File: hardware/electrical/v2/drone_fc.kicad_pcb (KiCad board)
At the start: 4 copper layers, 30 x 40.8 mm, 37 parts, among them J1 Cortex_SWD_10P, J2 ESC_4IN1_JST_SH, U1 TLV75533PDBVR, U2 LMR50410_Buck, U3 MDBT53-P1M, U4 ICM-42688-P

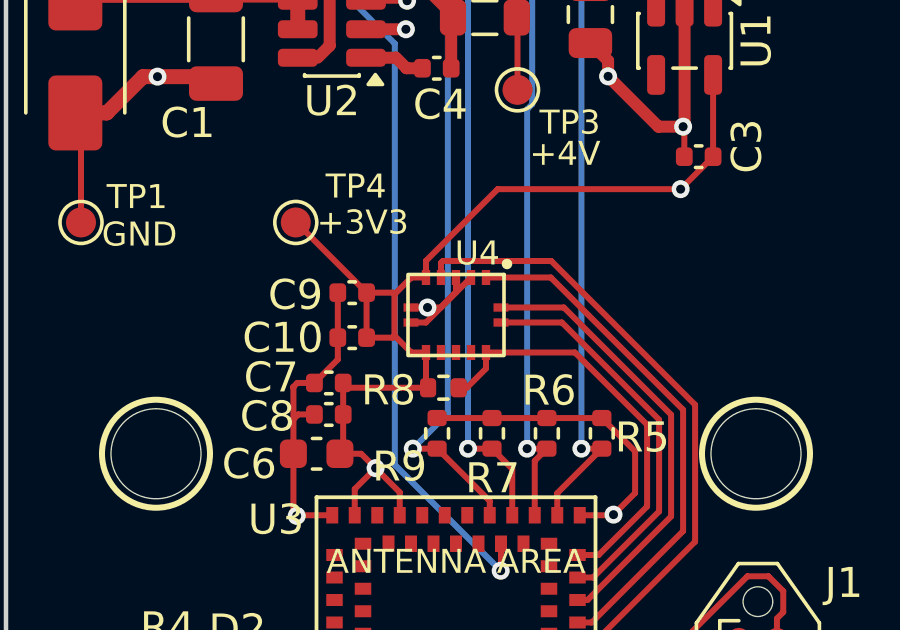
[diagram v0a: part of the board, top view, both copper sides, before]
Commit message: u4: fix ICM-42688-P footprint pad layout to match the datasheet
Pins 5 and 12 were placed as a 5th pad on the left/right edges
instead of on the bottom/top edges, giving a 5-5-2-2 pad distribution
across the four sides instead of the correct 4-3-4-3 (per Figure 5,
the pin-out diagram in DS-000347 rev 1.6, page 20). Text-extracting
the datasheet's pin table alone didn't catch this - it only confirmed
pin numbers map to the right signal names, not that the physical pad
positions matched the package outline. Rendering the actual diagram
page as an image caught the mismatch.

Moves pin 5 (VDDIO) onto the bottom edge and pin 12 (AP_CS) onto the
top edge, each at the correct 0.5 mm pitch alongside pins 6/7 and
13/14. Board re-routed for the two moved pads, including a GND via
that had ended up too close to the relocated pad 5.

ERC clean, DRC clean (0 errors, 0 unconnected).
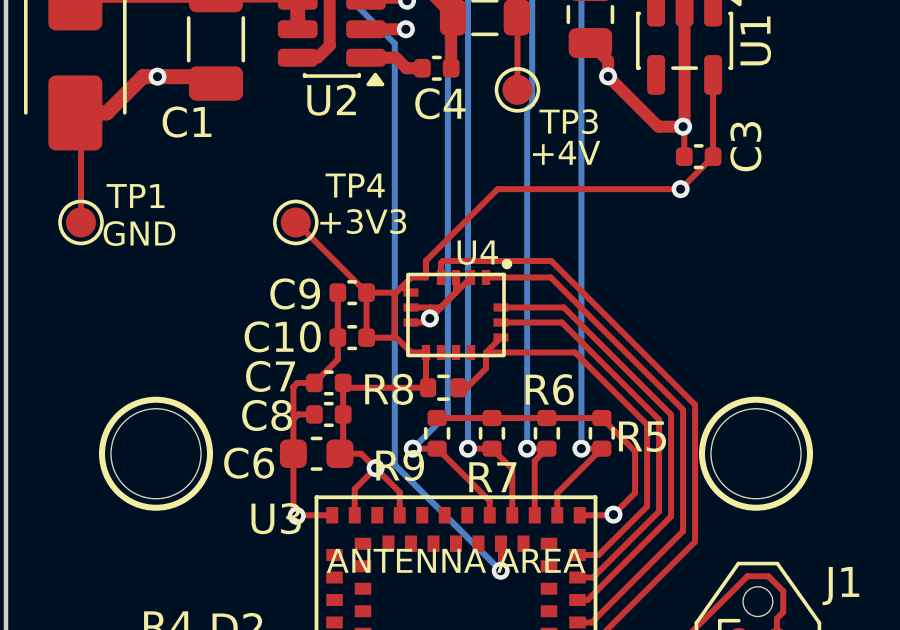
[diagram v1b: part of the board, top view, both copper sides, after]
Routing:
- net GND: track 69.5 -> 70.2 mm
- net /IMU_CS: track 13.8 -> 14.5 mm
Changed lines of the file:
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@@
 		(sheetname "/")
 		(sheetfile "drone_fc.kicad_sch")
-		(units
-			(unit
-				(name "A")
-				(pins "13" "1" "14" "12" "4" "9" "8" "5" "11" "2" "6" "7" "3" "10")
-			)
-		)
 		(attr smd)
 		(duplicate_pad_numbers_are_jumpers no)
@@
 		)
 		(pad "5" smd rect
-			(at -1.25 1 270)
-			(size 0.5 0.28)
+			(at -0.75 1.5 270)
+			(size 0.28 0.5)
 			(layers "F.Cu" "F.Mask" "F.Paste")
 			(net "/+3V3")
@@
 		)
 		(pad "12" smd rect
-			(at 1.25 -1 270)
-			(size 0.5 0.28)
+			(at 0.75 -1.5 270)
+			(size 0.28 0.5)
 			(layers "F.Cu" "F.Mask" "F.Paste")
 			(net "/IMU_CS")
@@
 	)
 	(segment
-		(start 98.5 105.125)
-		(end 99.05 105.125)
+		(start 94.57 107.78)
+		(end 94.58 107.79)
 		(width 0.2)
 		(layer "F.Cu")
@@
 	)
 	(segment
-		(start 94.57 107.78)
-		(end 94.58 107.79)
+		(start 99.49 105.12919)
+		(end 99.12919 105.49)
 		(width 0.2)
 		(layer "F.Cu")
@@
 	)
 	(segment
-		(start 100 104.615)
-		(end 100 104.125)
-		(width 0.2)
-		(layer "F.Cu")
-		(net "GND")
-	)
-	(segment
 		(start 94.74 108.69)
 		(end 94.58 108.85)
@@
 	)
 	(segment
-		(start 99.49 105.125)
-		(end 100 104.615)
+		(start 100 104.615)
+		(end 100 104.125)
 		(width 0.2)
 		(layer "F.Cu")
@@
 	)
 	(segment
+		(start 98.5 105.125)
+		(end 99.12919 105.125)
+		(width 0.2)
+		(layer "F.Cu")
+		(net "GND")
+	)
+	(segment
 		(start 96.06 106.13)
 		(end 96.06 104.63)
@@
 	)
 	(segment
+		(start 99.49 105.125)
+		(end 100 104.615)
+		(width 0.2)
+		(layer "F.Cu")
+		(net "GND")
+	)
+	(segment
 		(start 89.87 116.88)
 		(end 89.87 119.39)
@@
 	)
 	(segment
+		(start 99.49 105.125)
+		(end 99.49 105.12919)
+		(width 0.2)
+		(layer "F.Cu")
+		(net "GND")
+	)
+	(segment
 		(start 104.125 112.05)
 		(end 105.23 112.05)
@@
 	)
 	(segment
-		(start 99.05 105.125)
-		(end 99.49 105.125)
+		(start 94.58 110)
+		(end 94.58 111.96)
 		(width 0.2)
 		(layer "F.Cu")
@@
 	)
 	(segment
-		(start 94.58 110)
-		(end 94.58 111.96)
+		(start 99.12919 105.125)
+		(end 99.49 105.125)
 		(width 0.2)
 		(layer "F.Cu")
@@
 	)
 	(via
-		(at 99.05 105.125)
+		(at 105.31 121.25)
 		(size 0.6)
 		(drill 0.3)
@@
 	)
 	(via
-		(at 105.31 121.25)
+		(at 105.25 112.03)
 		(size 0.6)
 		(drill 0.3)
@@
 	)
 	(via
-		(at 105.25 112.03)
+		(at 99.12919 105.49)
 		(size 0.6)
 		(drill 0.3)
@@
 	)
 	(segment
+		(start 99.12919 105.49)
+		(end 99.32919 105.49)
+		(width 0.2)
+		(layer "B.Cu")
+		(net "GND")
+	)
+	(segment
 		(start 99 107.73)
 		(end 99 106.625)
@@
 	(segment
 		(start 98.51 104.125)
-		(end 97.95 104.685)
+		(end 98.2125 104.4225)
 		(width 0.2)
 		(layer "F.Cu")
@@
 	)
 	(segment
+		(start 98.5 104.625)
+		(end 98.415 104.625)
+		(width 0.2)
+		(layer "F.Cu")
+		(net "/+3V3")
+	)
+	(segment
 		(start 97.02 104.63)
 		(end 97.895 104.63)
@@
 		(net "/+3V3")
 	)
+	(segment
+		(start 98.415 104.625)
+		(end 98.2125 104.4225)
+		(width 0.2)
+		(layer "F.Cu")
+		(net "/+3V3")
+	)
+	(segment
+		(start 98.2125 104.4225)
+		(end 97.95 104.685)
+		(width 0.2)
+		(layer "F.Cu")
+		(net "/+3V3")
+	)
 	(via
 		(at 107.487556 101.18)
@@
 		(width 0.2)
 		(layer "F.Cu")
+		(net "/IMU_CS")
+	)
+	(segment
+		(start 101.5 106.125)
+		(end 101 106.625)
+		(width 0.2)
+		(layer "F.Cu")

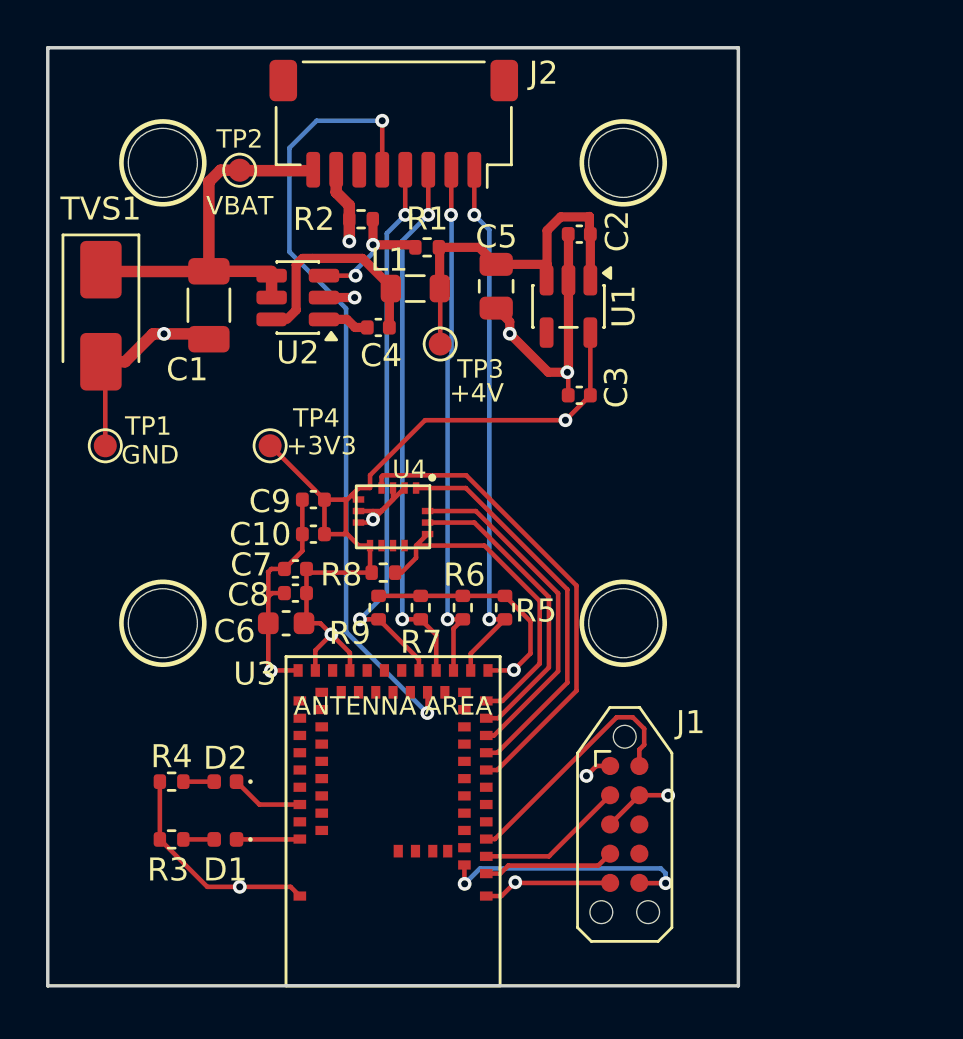
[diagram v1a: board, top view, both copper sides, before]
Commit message: u4: re-center IMU footprint pads and add a 3D model
Pin rows were shifted 0.25 mm off the package centerline on all four
edges (e.g. the left edge read -1.00/-0.50/0.00/+0.50 instead of the
symmetric -0.75/-0.25/+0.25/+0.75 a 0.5 mm pitch, 4-pin edge should
have). Found by rendering the mechanical drawing on page 55 of the
datasheet (DS-000347 rev 1.6) and comparing directly, rather than
trusting the pin-function table alone. Outer edge offsets (+-1.25 mm,
+-1.5 mm) already matched the 2.5x3.0 mm package half-dimensions and
were untouched.

Also adds a 3D model: no vendor STEP exists for the ICM-42688-P, so
this references KiCad's bundled generic LGA-14 3x2.5mm P0.5mm body
(Package_LGA.3dshapes, LayoutBorder3x4y - 3 pins on the short edges,
4 on the long edges, matching this part's pinout), rotated 90 degrees
to align its long axis with ours. Confirmed by render.

Board re-routed for the pad shift; a GND via that ended up too close
to the relocated pad 5 was moved clear. ERC clean, DRC clean (0
errors, 0 unconnected).
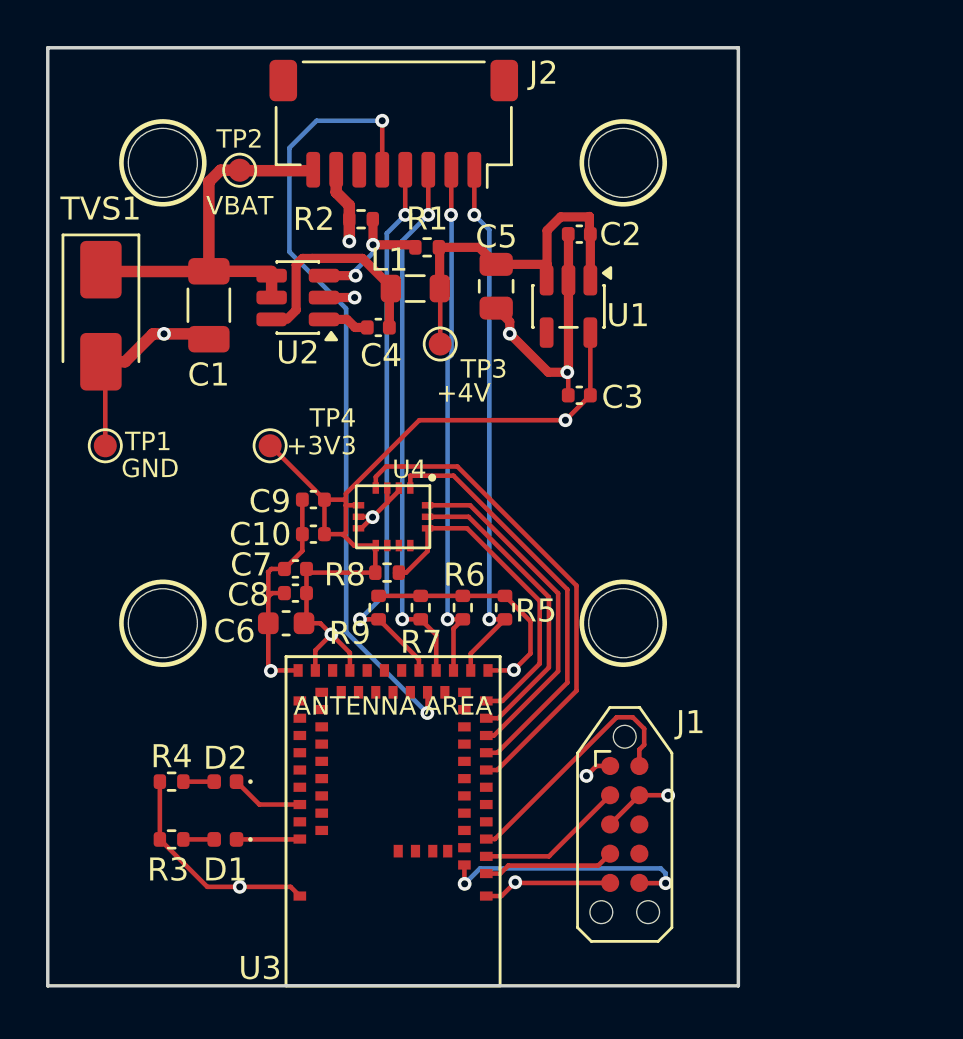
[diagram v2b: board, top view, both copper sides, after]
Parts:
- moved R8 0.16 mm to (99.7, 107.8)
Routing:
- net GND: track 70.2 -> 68.6 mm
- net /SPI_MISO: track 17.2 -> 18.2 mm
- net /IMU_INT1: track 20.9 -> 21.4 mm

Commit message: layout: add silkscreen text
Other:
- board text added: "${PROJECTNAME}"
- board text added: "NRP"
- board text added: "RADIO"
- board text added: "STATUS"
- board text added: "v1.0"
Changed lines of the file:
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@@
 		(layer "Edge.Cuts")
+	)
+	(gr_text "RADIO"
+		(at 89.39 114.95 0)
+		(layer "F.Cu")
+		(effects
+			(font
+				(size 1 1)
+				(thickness 0.15)
+				(bold yes)
+			)
+			(justify left bottom)
+		)
+	)
+	(gr_text ""
+		(at 108.2 104.99 0)
+		(layer "F.Cu")
+		(effects
+			(font
+				(size 1 1)
+				(thickness 0.15)
+				(bold yes)
+			)
+			(justify left bottom)
+		)
+	)
+	(gr_text "${PROJECTNAME}"
+		(at 107.94 103.59 0)
+		(layer "F.SilkS")
+		(effects
+			(font
+				(size 1 1)
+				(thickness 0.1)
+			)
+			(justify left bottom)
+		)
+	)
+	(gr_text "v1.0"
+		(at 107.94 105.065 0)
+		(layer "F.SilkS")
+		(effects
+			(font
+				(size 1 1)
+				(thickness 0.1)
+			)
+			(justify left bottom)
+		)
+	)
+	(gr_text "NRP"
+		(at 107.94 106.54 0)
+		(layer "F.SilkS")
+		(effects
+			(font
+				(size 1 1)
+				(thickness 0.1)
+			)
+			(justify left bottom)
+		)
+	)
+	(gr_text "STATUS"
+		(at 89.23 123.25 0)
+		(layer "F.SilkS")
+		(effects
+			(font
+				(size 1 1)
+				(thickness 0.15)
+				(bold yes)
+			)
+			(justify left bottom)
+		)
 	)
 	(segment

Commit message: hardware: sync PCB symbols and correct LED orientation
Apply the standard symbols and complete module pin metadata to the PCB. Rotate both LEDs to match their corrected polarity, move RADIO to silkscreen, and update the revision marking to v2.1.

Track, via and zone geometry is unchanged. Refilled-zone DRC finds no unconnected pads; only the existing silkscreen and mounting-hole warnings remain. Preserve the previously exported manufacturing files.
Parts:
- moved D1 0.06 mm to (92.7, 119.5), turned to 0 degrees
- turned D2 to 0 degrees
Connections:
- D1 pad 1: Net-(D1-A) -> Net-(D1-K)
- D1 pad 2: Net-(D1-K) -> /LED_STATUS
- D2 pad 1: Net-(D2-A) -> Net-(D2-K)
- D2 pad 2: Net-(D2-K) -> /LED_RADIO
- J1 pad 7: (no net) -> unconnected-(J1-KEY-Pad7)
- J1 pad 8: (no net) -> unconnected-(J1-NC/TDI-Pad8)
- U3 pad 10: (no net) -> unconnected-(U3B-P1.06-Pad10)
- U3 pad 11: (no net) -> unconnected-(U3B-P1.04-Pad11)
- U3 pad 12: (no net) -> unconnected-(U3B-P0.21-Pad12)
- U3 pad 13: (no net) -> unconnected-(U3B-P0.20-Pad13)
- U3 pad 15: (no net) -> unconnected-(U3B-P0.12-Pad15)
- U3 pad 17: (no net) -> unconnected-(U3B-P0.11-Pad17)
- U3 pad 19: (no net) -> unconnected-(U3B-P0.09-Pad19)
- U3 pad 21: (no net) -> unconnected-(U3B-P0.13-Pad21)
- U3 pad 23: (no net) -> unconnected-(U3B-P0.15-Pad23)
- U3 pad 27: (no net) -> unconnected-(U3B-P0.14-Pad27)
- U3 pad 31: (no net) -> unconnected-(U3B-P1.03-Pad31)
- U3 pad 32: (no net) -> unconnected-(U3B-P0.02-Pad32)
- U3 pad 33: (no net) -> unconnected-(U3B-P1.02-Pad33)
- U3 pad 34: (no net) -> unconnected-(U3B-P0.00-Pad34)
- U3 pad 35: (no net) -> unconnected-(U3B-P0.06-Pad35)
- U3 pad 36: (no net) -> unconnected-(U3B-P0.01-Pad36)
- U3 pad 39: (no net) -> unconnected-(U3B-P0.05-Pad39)
- U3 pad 40: (no net) -> unconnected-(U3C-DCCH-Pad40)
- U3 pad 43: (no net) -> unconnected-(U3B-P1.01-Pad43)
- U3 pad 45: (no net) -> unconnected-(U3B-P1.00-Pad45)
- U3 pad 47: (no net) -> unconnected-(U3B-P1.15-Pad47)
- U3 pad 49: (no net) -> unconnected-(U3B-P1.14-Pad49)
- U3 pad 50: (no net) -> unconnected-(U3C-DCCD-Pad50)
- U3 pad 51: (no net) -> unconnected-(U3B-P1.13-Pad51)
- U3 pad 52: (no net) -> unconnected-(U3C-DECD-Pad52)
- U3 pad 53: (no net) -> unconnected-(U3B-P1.12-Pad53)
- U3 pad 54: (no net) -> unconnected-(U3C-DCC-Pad54)
- U3 pad 55: (no net) -> unconnected-(U3B-P1.11-Pad55)
- U3 pad 56: Net-(D2-A) -> /LED_RADIO
- U3 pad 57: (no net) -> unconnected-(U3B-P0.30-Pad57)
- U3 pad 58: (no net) -> unconnected-(U3C-DECR-Pad58)
- U3 pad 59: (no net) -> unconnected-(U3B-P1.10-Pad59)
- U3 pad 60: Net-(D1-A) -> /LED_STATUS
- U3 pad 62: (no net) -> unconnected-(U3B-P0.23-Pad62)
- U3 pad 63: (no net) -> unconnected-(U3B-P1.07-Pad63)
- U3 pad 64: (no net) -> unconnected-(U3B-P1.09-Pad64)
- U3 pad 65: (no net) -> unconnected-(U3B-P0.29-Pad65)
- U3 pad 7: (no net) -> unconnected-(U3B-P0.26-Pad7)
- U3 pad 8: (no net) -> unconnected-(U3B-P0.24-Pad8)
- U3 pad 9: (no net) -> unconnected-(U3B-P0.25-Pad9)
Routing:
- net Net-(D2-A): track 3.16 -> 0.00 mm
- net /LED_RADIO: track 0.00 -> 3.16 mm
- net Net-(D1-A): track 2.73 -> 0.00 mm
- net /LED_STATUS: track 0.00 -> 2.73 mm
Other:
- board text added: "v2.1"
- board text removed: "v1.0"
